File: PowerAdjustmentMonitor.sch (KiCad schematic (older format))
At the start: 37 parts, among them U3 LM317T, U4 LM317T, U5 LM337T, U6 LM337T

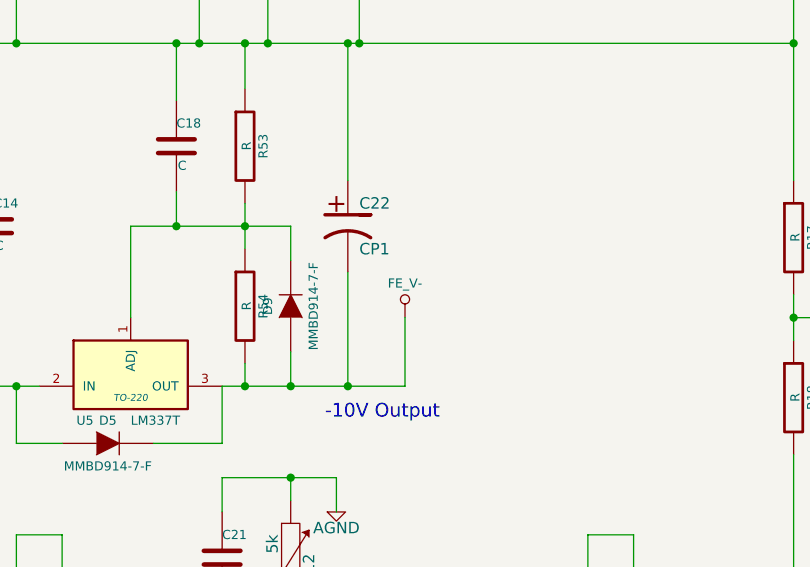
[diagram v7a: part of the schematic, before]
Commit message: Various minor updates after Ground and Power Planes video
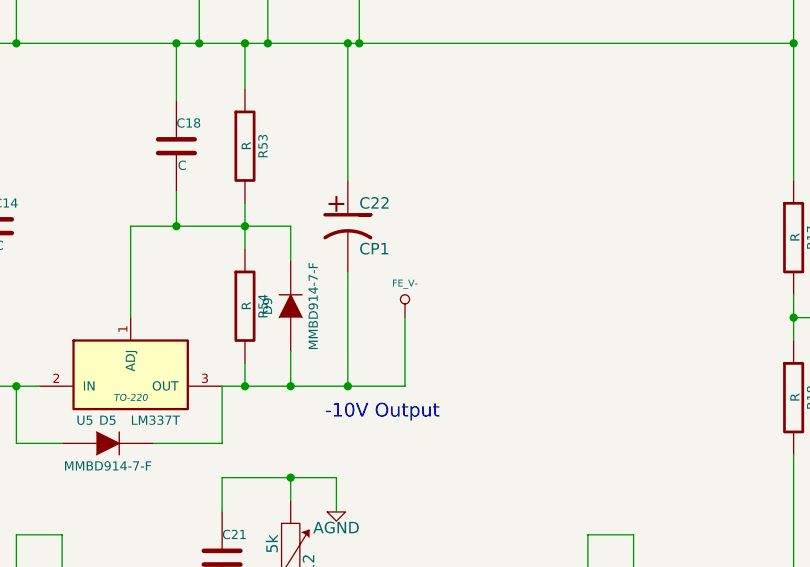
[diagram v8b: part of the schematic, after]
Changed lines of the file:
@@
 $EndDescr
 $Comp
-L +3.3V #PWR025
+L +3.3V #PWR40
 U 1 1 52F2A379
 P 9700 2000
-F 0 "#PWR025" H 9700 1960 30  0001 C CNN
+F 0 "#PWR40" H 9700 1960 30  0001 C CNN
 F 1 "+3.3V" H 9700 2110 30  0000 C CNN
 F 2 "" H 9700 2000 60  0000 C CNN
@@
 $EndComp
 $Comp
-L +5V #PWR026
+L +5V #PWR39
 U 1 1 52F2A37F
 P 9500 2000
-F 0 "#PWR026" H 9500 2090 20  0001 C CNN
+F 0 "#PWR39" H 9500 2090 20  0001 C CNN
 F 1 "+5V" H 9500 2090 30  0000 C CNN
 F 2 "" H 9500 2000 60  0000 C CNN
@@
 $EndComp
 $Comp
-L +12V #PWR027
+L +12V #PWR28
 U 1 1 52F2A40B
 P 2200 2400
-F 0 "#PWR027" H 2200 2350 20  0001 C CNN
+F 0 "#PWR28" H 2200 2350 20  0001 C CNN
 F 1 "+12V" H 2200 2500 30  0000 C CNN
 F 2 "" H 2200 2400 60  0000 C CNN
@@
 $EndComp
 $Comp
-L -12V #PWR028
+L -12V #PWR29
 U 1 1 52F2A411
 P 2200 5400
-F 0 "#PWR028" H 2200 5530 20  0001 C CNN
+F 0 "#PWR29" H 2200 5530 20  0001 C CNN
 F 1 "-12V" H 2200 5500 30  0000 C CNN
 F 2 "" H 2200 5400 60  0000 C CNN
@@
 $EndComp
 $Comp
-L GND #PWR029
+L GND #PWR26
 U 1 1 52F2A4F6
 P 1250 4300
-F 0 "#PWR029" H 1250 4300 30  0001 C CNN
+F 0 "#PWR26" H 1250 4300 30  0001 C CNN
 F 1 "GND" H 1250 4230 30  0001 C CNN
 F 2 "" H 1250 4300 60  0000 C CNN
@@
 $EndComp
 $Comp
-L AGND #PWR030
+L AGND #PWR27
 U 1 1 52F2A718
 P 1850 4300
-F 0 "#PWR030" H 1850 4300 40  0001 C CNN
+F 0 "#PWR27" H 1850 4300 40  0001 C CNN
 F 1 "AGND" H 1850 4230 50  0000 C CNN
 F 2 "" H 1850 4300 60  0000 C CNN
@@
 $EndComp
 $Comp
-L AGND #PWR031
+L AGND #PWR30
 U 1 1 52F2A798
 P 2500 4300
-F 0 "#PWR031" H 2500 4300 40  0001 C CNN
+F 0 "#PWR30" H 2500 4300 40  0001 C CNN
 F 1 "AGND" H 2500 4230 50  0000 C CNN
 F 2 "" H 2500 4300 60  0000 C CNN
@@
 $EndComp
 $Comp
-L FE_V+ #PWR032
+L FE_V+ #PWR35
 U 1 1 52F2A802
 P 4500 2400
-F 0 "#PWR032" H 4500 2500 30  0001 C CNN
+F 0 "#PWR35" H 4500 2500 30  0001 C CNN
 F 1 "FE_V+" H 4500 2500 30  0000 C CNN
 F 2 "" H 4500 2400 60  0000 C CNN
 F 3 "" H 4500 2400 60  0000 C CNN
 	1    4500 2400
-	1    0    0    -1
-$EndComp
-$Comp
-L FE_V- #PWR36
-U 1 1 52F2A839
-P 4500 5300
-F 0 "#PWR36" H 4500 5500 40  0001 C CNN
-F 1 "FE_V-" H 4500 5450 40  0000 C CNN
-F 2 "" H 4500 5300 60  0000 C CNN
-F 3 "" H 4500 5300 60  0000 C CNN
-	1    4500 5300
 	1    0    0    -1
 $EndComp
@@
 $EndComp
 $Comp
-L AGND #PWR033
+L AGND #PWR38
 U 1 1 52F2A9E8
 P 5500 6400
-F 0 "#PWR033" H 5500 6400 40  0001 C CNN
+F 0 "#PWR38" H 5500 6400 40  0001 C CNN
 F 1 "AGND" H 5500 6330 50  0000 C CNN
 F 2 "" H 5500 6400 60  0000 C CNN
@@
 $EndComp
 $Comp
-L AGND #PWR034
+L AGND #PWR33
 U 1 1 52F2AAAD
 P 4000 2200
-F 0 "#PWR034" H 4000 2200 40  0001 C CNN
+F 0 "#PWR33" H 4000 2200 40  0001 C CNN
 F 1 "AGND" H 4000 2130 50  0000 C CNN
 F 2 "" H 4000 2200 60  0000 C CNN
@@
 	4000 2100 4000 2200
 $Comp
-L AGND #PWR035
+L AGND #PWR31
 U 1 1 530A4A4A
 P 2800 1700
-F 0 "#PWR035" H 2800 1700 40  0001 C CNN
+F 0 "#PWR31" H 2800 1700 40  0001 C CNN
 F 1 "AGND" H 2800 1630 50  0000 C CNN
 F 2 "" H 2800 1700 60  0000 C CNN
@@
 	2800 1700 2800 1600
 $Comp
-L AGND #PWR036
+L AGND #PWR37
 U 1 1 530A4AF9
 P 5300 1700
-F 0 "#PWR036" H 5300 1700 40  0001 C CNN
+F 0 "#PWR37" H 5300 1700 40  0001 C CNN
 F 1 "AGND" H 5300 1630 50  0000 C CNN
 F 2 "" H 5300 1700 60  0000 C CNN
@@
 	5300 6250 5300 6600
 $Comp
-L AGND #PWR037
+L AGND #PWR32
 U 1 1 530A4E0D
 P 3000 6400
-F 0 "#PWR037" H 3000 6400 40  0001 C CNN
+F 0 "#PWR32" H 3000 6400 40  0001 C CNN
 F 1 "AGND" H 3000 6330 50  0000 C CNN
 F 2 "" H 3000 6400 60  0000 C CNN
@@
 	2800 6250 2800 6600
 $Comp
-L AGND #PWR038
+L AGND #PWR34
 U 1 1 530A4E16
 P 4200 6150
-F 0 "#PWR038" H 4200 6150 40  0001 C CNN
+F 0 "#PWR34" H 4200 6150 40  0001 C CNN
 F 1 "AGND" H 4200 6080 50  0000 C CNN
 F 2 "" H 4200 6150 60  0000 C CNN
@@
 	3800 7650 3800 7400
 Connection ~ 3800 7400
+$Comp
+L FE_V- #PWR36
+U 1 1 530BD9FD
+P 4500 5300
+F 0 "#PWR36" H 4500 5500 40  0001 C CNN
+F 1 "FE_V-" H 4500 5450 30  0000 C CNN
+F 2 "" H 4500 5300 60  0000 C CNN
+F 3 "" H 4500 5300 60  0000 C CNN
+	1    4500 5300
+	1    0    0    -1
+$EndComp
 $EndSCHEMATC
